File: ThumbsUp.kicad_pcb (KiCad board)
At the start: 2 copper layers, 395.5 x 277.7 mm, 210 parts, among them IC1 RP2040, IC2 W25Q128JVSIM, IC3 RP2040, IC4 W25Q128JVSIM, J1 Conn_01x04_Male, J10 Raiser_Male, J11 Raiser_Female, J12 Raiser_Male, J13 Raiser_Female, J14 Raiser_Male, J15 Raiser_Female, J16 Raiser_Male, J17 Raiser_Female, J18 Raiser_Male, J19 Raiser_Female, J2 Conn_01x04_Male, J20 Conn_01x04_Female, J21 Conn_01x04_Female, J22 Conn_01x04_Female, J23 Conn_01x04_Female, J24 Conn_01x04_Male, J25 Conn_01x04_Male, J26 Conn_01x04_Male, J27 Conn_01x04_Male, J28 Conn_01x04_Female, J29 Conn_01x04_Female, J3 Conn_01x04_Female, J30 Conn_01x04_Female, J31 Conn_01x04_Female, J32 USB_C_Receptacle_USB2.0, J33 Raiser_Male, J34 Raiser_Female, J35 Raiser_Male, J36 PJ-3200B, J37 USB_C_Receptacle_USB2.0, J38 Raiser_Female, J39 Raiser_Male, J4 Conn_01x04_Male, J40 Raiser_Female, J41 Raiser_Male, J42 Raiser_Female, J43 Raiser_Male, J44 Raiser_Female, J45 Raiser_Male, J46 PJ-3200B, J47 Raiser_Female, J48 Raiser_Male, J49 Raiser_Female, J5 Conn_01x04_Female, J50 Raiser_Male, J51 Raiser_Female, J52 Raiser_Male, J55 Conn_01x04_Male, J6 Conn_01x04_Male, J7 Conn_01x04_Male, J8 Conn_01x04_Male, J9 Raiser_Female, U1 AMS1117-3.3_SOT223, U2 AMS1117-3.3_SOT223, Y1 ABLS-12.000MHZ-B4-T, Y2 ABLS-12.000MHZ-B4-T

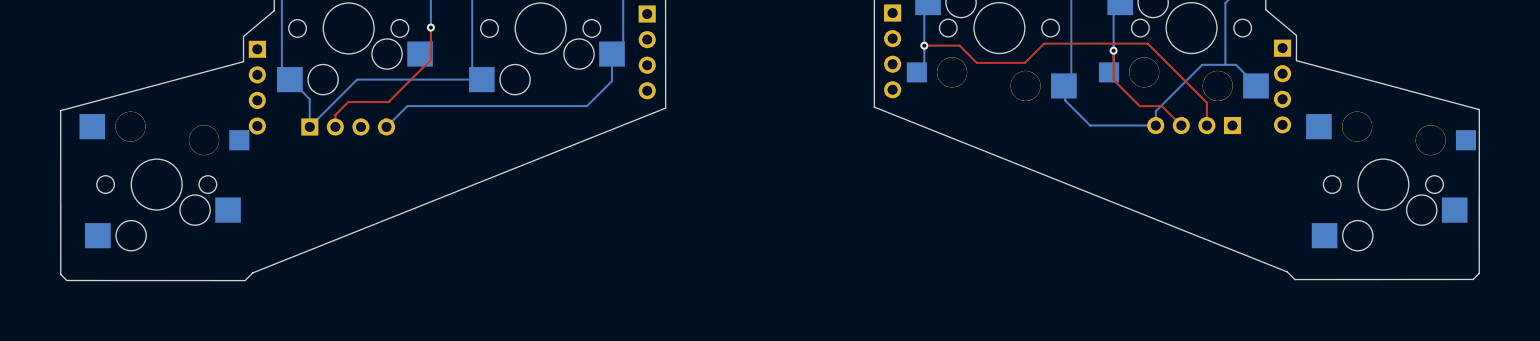
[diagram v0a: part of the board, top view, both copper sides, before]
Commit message: Adding the 3key thumbclusters
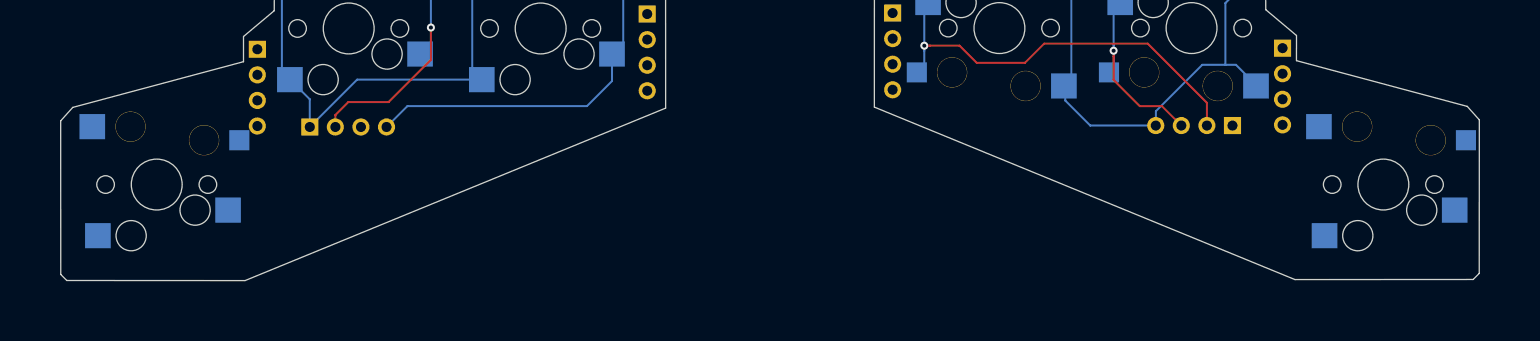
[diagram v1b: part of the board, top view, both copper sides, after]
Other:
- outline, holes or cut-outs redrawn
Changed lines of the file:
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@@
     (aux_axis_origin 0 0)
     (grid_origin 166.8 443.6)
-    (visible_elements 7FFFFFFF)
+    (visible_elements 7FFFF7FF)
     (pcbplotparams
       (layerselection 0x010fc_ffffffff)
@@
     )
   )
+  (gr_line (start 21.830195 401.078102) (end 23.030195 402.418102) (layer Edge.Cuts) (width 0.05))
+  (gr_line (start 23.030195 402.418102) (end 23.020195 417.668102) (layer Edge.Cuts) (width 0.05))
+  (gr_line (start 4.870195 396.538102) (end 21.830195 401.078102) (layer Edge.Cuts) (width 0.05))
+  (gr_line (start -116.66 401.18) (end -117.86 402.52) (layer Edge.Cuts) (width 0.05))
   (gr_line (start -38.149804 456.568103) (end -53.129804 456.558103) (layer Edge.Cuts) (width 0.05))
   (gr_line (start -53.849804 457.278103) (end -53.849804 474.838103) (layer Edge.Cuts) (width 0.05))
@@
   (gr_line (start -87.96 456.67) (end -72.98 456.66) (layer Edge.Cuts) (width 0.05))
   (gr_line (start -88.423847 456.271308) (end -87.96 456.67) (layer Edge.Cuts) (width 0.05))
-  (gr_line (start -37.051253 401.149426) (end 3.960195 417.518102) (layer Edge.Cuts) (width 0.05))
+  (gr_line (start -37.051253 401.149426) (end 4.720195 418.278102) (layer Edge.Cuts) (width 0.05))
   (gr_line (start 4.870195 396.538102) (end 4.871005 394.036601) (layer Edge.Cuts) (width 0.05))
-  (gr_line (start 4.720195 418.278102) (end 3.960195 417.518102) (layer Edge.Cuts) (width 0.05))
   (gr_line (start 23.020195 417.668102) (end 22.420195 418.268102) (layer Edge.Cuts) (width 0.05))
   (gr_line (start 22.420195 418.268102) (end 4.720195 418.278102) (layer Edge.Cuts) (width 0.05))
-  (gr_line (start 23.030195 401.398102) (end 23.020195 417.668102) (layer Edge.Cuts) (width 0.05))
-  (gr_line (start 4.870195 396.538102) (end 23.030195 401.398102) (layer Edge.Cuts) (width 0.05))
-  (gr_line (start -99.55 418.38) (end -98.79 417.62) (layer Edge.Cuts) (width 0.05))
   (gr_line (start -117.25 418.37) (end -99.55 418.38) (layer Edge.Cuts) (width 0.05))
   (gr_line (start -117.85 417.77) (end -117.25 418.37) (layer Edge.Cuts) (width 0.05))
-  (gr_line (start -117.86 401.5) (end -117.85 417.77) (layer Edge.Cuts) (width 0.05))
-  (gr_line (start -99.7 396.64) (end -117.86 401.5) (layer Edge.Cuts) (width 0.05))
+  (gr_line (start -117.86 402.52) (end -117.85 417.77) (layer Edge.Cuts) (width 0.05))
+  (gr_line (start -99.7 396.64) (end -116.66 401.18) (layer Edge.Cuts) (width 0.05))
   (gr_line (start -25.711253 364.399426) (end -24.111253 362.799426) (layer Edge.Cuts) (width 0.05))
   (gr_line (start -24.111253 362.799426) (end -21.211253 352.699426) (layer Edge.Cuts) (width 0.05))
@@
   (gr_line (start -57.778552 401.251324) (end -57.783847 390.111308) (layer Edge.Cuts) (width 0.05))
   (gr_line (start -37.051253 401.149426) (end -37.045957 390.009411) (layer Edge.Cuts) (width 0.05))
-  (gr_line (start -57.778552 401.251324) (end -98.79 417.62) (layer Edge.Cuts) (width 0.05))
+  (gr_line (start -57.778552 401.251324) (end -99.55 418.38) (layer Edge.Cuts) (width 0.05))
   (gr_line (start 0.248753 386.05148) (end 1.806995 387.552472) (layer Edge.Cuts) (width 0.05))
   (gr_line (start -34.157244 386.17596) (end -32.251197 379.110269) (layer Edge.Cuts) (width 0.05))

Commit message: Tracedd the 3key thumbclusters
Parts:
- removed the J10 at (-129.0, 461.6)
- removed the J10 at (-98.3, 395.4)
- removed the J10 at (-87.5, 342.2)
- removed the J14 at (-90.2, 458.1)
- removed the J14 at (-59.6, 391.9)
- removed the J14 at (-48.8, 338.7)
- removed the J18 at (-102.8, 447.6)
- removed the J18 at (-72.2, 381.4)
- removed the J18 at (-61.4, 328.2)
- removed the J33 at (2.85, 461.5)
- removed the J33 at (3.49, 395.3)
- removed the J33 at (-4.68, 342.1)
- removed the J35 at (-23.3, 447.5)
- removed the J35 at (-22.7, 381.3)
- removed the J35 at (-30.9, 328.2)
- removed the J4 at (-123.8, 469.3)
- removed the J4 at (-93.1, 403.1)
- removed the J48 at (-35.9, 458.0)
- removed the J48 at (-35.2, 391.8)
- removed the J48 at (-43.4, 338.7)
- removed the J6 at (-2.12, 469.1)
- removed the J6 at (-1.48, 403.0)
- removed the J6 at (-9.65, 349.8)
- removed the MX18 at (-100.8, 459.5)
- removed the MX18 at (-70.2, 393.3)
- removed the MX18 at (-59.4, 337.0)
- removed the MX22 at (-119.9, 459.5)
- removed the MX22 at (-89.3, 393.3)
- removed the MX22 at (-78.5, 340.1)
- removed the MX26 at (-6.23, 459.5)
- removed the MX26 at (-5.55, 393.3)
- removed the MX26 at (-13.6, 340.2)
- removed the MX30 at (-25.3, 459.5)
- removed the MX30 at (-24.6, 393.3)
- removed the MX30 at (-32.7, 337.0)
- added J53: Conn_01x04_Male, Connector_PinHeader_2.54mm:PinHeader_1x04_P2.54mm_Vertical, B.Cu at (-93.1, 403.1)
- added J54: Conn_01x04_Male, Connector_PinHeader_2.54mm:PinHeader_1x04_P2.54mm_Vertical, B.Cu at (-123.8, 469.3)
- added J56: Conn_01x04_Male, Connector_PinHeader_2.54mm:PinHeader_1x04_P2.54mm_Vertical, B.Cu at (-1.48, 403.0)
- added J57: Conn_01x04_Male, Connector_PinHeader_2.54mm:PinHeader_1x04_P2.54mm_Vertical, B.Cu at (-2.12, 469.1)
- added J58: Conn_01x04_Male, Connector_PinHeader_2.54mm:PinHeader_1x04_P2.54mm_Vertical, B.Cu at (-9.65, 349.8)
- added J59: Raiser_Male, Connector_PinHeader_2.54mm:PinHeader_1x04_P2.54mm_Vertical, B.Cu at (-87.5, 342.2)
- added J60: Raiser_Male, Connector_PinHeader_2.54mm:PinHeader_1x04_P2.54mm_Vertical, B.Cu at (-61.4, 328.2)
- added J61: Raiser_Male, Connector_PinHeader_2.54mm:PinHeader_1x04_P2.54mm_Vertical, B.Cu at (-48.8, 338.7)
- added J62: Raiser_Male, Connector_PinHeader_2.54mm:PinHeader_1x04_P2.54mm_Vertical, B.Cu at (-43.4, 338.7)
- added J63: Raiser_Male, Connector_PinHeader_2.54mm:PinHeader_1x04_P2.54mm_Vertical, B.Cu at (-30.9, 328.2)
- added J64: Raiser_Male, Connector_PinHeader_2.54mm:PinHeader_1x04_P2.54mm_Vertical, B.Cu at (-4.68, 342.1)
- added J65: Raiser_Male, Connector_PinHeader_2.54mm:PinHeader_1x04_P2.54mm_Vertical, B.Cu at (-98.3, 395.4)
- added J66: Raiser_Male, Connector_PinHeader_2.54mm:PinHeader_1x04_P2.54mm_Vertical, B.Cu at (-72.2, 381.4)
- added J67: Raiser_Male, Connector_PinHeader_2.54mm:PinHeader_1x04_P2.54mm_Vertical, B.Cu at (-59.6, 391.9)
- added J68: Raiser_Male, Connector_PinHeader_2.54mm:PinHeader_1x04_P2.54mm_Vertical, B.Cu at (-35.2, 391.8)
- added J69: Raiser_Male, Connector_PinHeader_2.54mm:PinHeader_1x04_P2.54mm_Vertical, B.Cu at (-22.7, 381.3)
- added J70: Raiser_Male, Connector_PinHeader_2.54mm:PinHeader_1x04_P2.54mm_Vertical, B.Cu at (3.49, 395.3)
- added J71: Raiser_Male, Connector_PinHeader_2.54mm:PinHeader_1x04_P2.54mm_Vertical, B.Cu at (-129.0, 461.6)
- added J72: Raiser_Male, Connector_PinHeader_2.54mm:PinHeader_1x04_P2.54mm_Vertical, B.Cu at (-102.8, 447.6)
- added J73: Raiser_Male, Connector_PinHeader_2.54mm:PinHeader_1x04_P2.54mm_Vertical, B.Cu at (-90.2, 458.1)
- added J74: Raiser_Male, Connector_PinHeader_2.54mm:PinHeader_1x04_P2.54mm_Vertical, B.Cu at (-35.9, 458.0)
- added J75: Raiser_Male, Connector_PinHeader_2.54mm:PinHeader_1x04_P2.54mm_Vertical, B.Cu at (-23.3, 447.5)
- added J76: Raiser_Male, Connector_PinHeader_2.54mm:PinHeader_1x04_P2.54mm_Vertical, B.Cu at (2.85, 461.5)
- added MX57: SwThL, keyswitches:MX-GLP2-HotSwap, F.Cu at (69.1, 354.5)
- added MX58: SwThR, keyswitches:MX-GLP2-HotSwap, F.Cu at (228.3, 352.1)
- added MX59: SwLSHFT, keyswitches:MX-GLP2-HotSwap, F.Cu at (-89.3, 393.3)
- added MX60: SwLSHFT, keyswitches:MX-GLP2-HotSwap, F.Cu at (-119.9, 459.5)
- added MX61: SwLSHFT, keyswitches:MX-GLP2-HotSwap, F.Cu at (-78.5, 340.1)
- added MX62: SwLMOD, keyswitches:MX-GLP2-HotSwap, F.Cu at (-70.2, 393.3)
- added MX63: SwLMOD, keyswitches:MX-GLP2-HotSwap, F.Cu at (-100.8, 459.5)
- added MX64: SwLMOD, keyswitches:MX-GLP2-HotSwap, F.Cu at (-59.4, 337.0)
- added MX71: SwRMOD, keyswitches:MX-GLP2-HotSwap, F.Cu at (-24.6, 393.3)
- added MX72: SwRMOD, keyswitches:MX-GLP2-HotSwap, F.Cu at (-25.3, 459.5)
- added MX73: SwRMOD, keyswitches:MX-GLP2-HotSwap, F.Cu at (-32.7, 337.0)
- added MX74: SwRSHFT, keyswitches:MX-GLP2-HotSwap, F.Cu at (-5.55, 393.3)
- added MX75: SwRSHFT, keyswitches:MX-GLP2-HotSwap, F.Cu at (-6.23, 459.5)
- added MX76: SwRSHFT, keyswitches:MX-GLP2-HotSwap, F.Cu at (-13.6, 340.2)
- moved C20 0.07 mm to (166.6, 460.1)
- moved C26 0.07 mm to (166.6, 459.1)
- renumbered MX57 to MX65, MX57 to MX66, MX57 to MX67, MX58 to MX68, MX58 to MX69, MX58 to MX70
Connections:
- J10 pad 1: Net-(J10-Pad1) -> (no net)
- J10 pad 2: Net-(J10-Pad2) -> (no net)
- J10 pad 3: Net-(J10-Pad3) -> (no net)
- J10 pad 4: Net-(J10-Pad4) -> (no net)
- J14 pad 1: Net-(J14-Pad1) -> (no net)
- J14 pad 2: Net-(J14-Pad2) -> (no net)
- J14 pad 3: Net-(J14-Pad3) -> (no net)
- J14 pad 4: Net-(J14-Pad4) -> (no net)
- J18 pad 1: Net-(J18-Pad1) -> (no net)
- J18 pad 2: Net-(J18-Pad2) -> (no net)
- J18 pad 3: Net-(J18-Pad3) -> (no net)
- J18 pad 4: Net-(J18-Pad4) -> (no net)
- J33 pad 1: Net-(J33-Pad1) -> (no net)
- J33 pad 2: Net-(J33-Pad2) -> (no net)
- J33 pad 3: Net-(J33-Pad3) -> (no net)
- J33 pad 4: Net-(J33-Pad4) -> (no net)
- J35 pad 1: Net-(J35-Pad1) -> (no net)
- J35 pad 2: Net-(J35-Pad2) -> (no net)
- J35 pad 3: Net-(J35-Pad3) -> (no net)
- J35 pad 4: Net-(J35-Pad4) -> (no net)
- J48 pad 1: Net-(J48-Pad1) -> (no net)
- J48 pad 2: Net-(J48-Pad2) -> (no net)
- J48 pad 3: Net-(J48-Pad3) -> (no net)
- J48 pad 4: Net-(J48-Pad4) -> (no net)
- J55 pad 1: Net-(J4-Pad1) -> Net-(J55-Pad1)
- J55 pad 2: Net-(J4-Pad2) -> Net-(J55-Pad2)
- J55 pad 3: Net-(J4-Pad3) -> Net-(J55-Pad3)
- J55 pad 4: Net-(J4-Pad4) -> Net-(J55-Pad4)
- MX65 pad 1: Net-(J4-Pad1) -> Net-(J53-Pad1)
- MX65 pad 2: Net-(J4-Pad3) -> Net-(J53-Pad3)
- MX66 pad 1: Net-(J4-Pad1) -> Net-(J54-Pad1)
- MX66 pad 2: Net-(J4-Pad3) -> Net-(J54-Pad3)
- MX67 pad 1: Net-(J4-Pad1) -> Net-(J55-Pad1)
- MX67 pad 2: Net-(J4-Pad3) -> Net-(J55-Pad3)
- MX68 pad 1: Net-(J6-Pad4) -> Net-(J56-Pad4)
- MX68 pad 2: Net-(J6-Pad1) -> Net-(J56-Pad1)
- MX69 pad 1: Net-(J6-Pad4) -> Net-(J57-Pad4)
- MX69 pad 2: Net-(J6-Pad1) -> Net-(J57-Pad1)
- MX70 pad 1: Net-(J6-Pad4) -> Net-(J58-Pad4)
- MX70 pad 2: Net-(J6-Pad1) -> Net-(J58-Pad1)
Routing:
- net Net-(J4-Pad1): track 224.1 -> 59.2 mm, vias 2 -> 0
- net Net-(J6-Pad4): track 217.6 -> 58.2 mm
- net Net-(J6-Pad2): track 166.5 -> 41.7 mm, vias 4 -> 1
- net Net-(J4-Pad4): track 125.7 -> 34.4 mm, vias 1 -> 0
- net Net-(J53-Pad1): track 0.00 -> 83.4 mm
- net Net-(J54-Pad1): track 0.00 -> 82.6 mm, vias 0 -> 2
- net Net-(J57-Pad4): track 0.00 -> 81.5 mm
- net Net-(J55-Pad1): track 0.00 -> 79.5 mm, vias 0 -> 2
- net Net-(J58-Pad4): track 0.00 -> 76.2 mm
- net Net-(J4-Pad2): track 94.2 -> 23.6 mm, vias 4 -> 1
- net Net-(J56-Pad4): track 0.00 -> 67.6 mm
- net Net-(J57-Pad1): track 0.00 -> 59.8 mm, vias 0 -> 2
- net Net-(J6-Pad3): track 76.8 -> 18.9 mm, vias 4 -> 1
- net Net-(J54-Pad3): track 0.00 -> 55.9 mm, vias 0 -> 1
- net Net-(J57-Pad2): track 0.00 -> 41.7 mm, vias 0 -> 1
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
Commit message: Put the silkscreens on, ready for Gerbers creation
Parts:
- added G***: LOGO, Silkscreens:Crowfeet75, B.Cu at (138.4, 567.7)
- added G***: LOGO, Silkscreens:Crowfeet75, F.Cu at (-145.4, 409.6)
- added G***: LOGO, Silkscreens:Crowfeet75, F.Cu at (141.0, 404.6)
- added G***: LOGO, Silkscreens:Crowfeet75, F.Cu at (138.5, 564.2)
- moved MX64 49.9 mm to (-106.8, 352.4)
- moved MX67 49.9 mm to (-106.8, 371.5)
- moved J55 49.9 mm to (-129.8, 365.3)
- moved J60 49.9 mm to (-108.9, 343.7)
- moved J61 49.9 mm to (-96.3, 354.1)
- moved J63 49.9 mm to (-78.3, 343.6)
- moved MX61 49.9 mm to (-125.9, 355.6)
- moved MX70 49.9 mm to (-80.1, 371.5)
- moved MX73 49.9 mm to (-80.1, 352.4)
- moved J62 49.9 mm to (-90.8, 354.1)
- moved J58 49.9 mm to (-57.1, 365.3)
- moved J59 49.9 mm to (-135.0, 357.6)
- moved J64 49.9 mm to (-52.1, 357.6)
- moved MX76 49.9 mm to (-61.0, 355.6)
- moved MX59 48.9 mm to (-136.2, 407.3)
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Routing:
- net Net-(J23-Pad3): track 41.2 -> 42.3 mm
- net Net-(J15-Pad3): track 96.9 -> 98.0 mm
- net Net-(J44-Pad4): track 69.5 -> 68.6 mm
- net Net-(J44-Pad2): track 102.6 -> 101.8 mm
- net Net-(J44-Pad1): track 136.5 -> 135.7 mm
- net Net-(J44-Pad3): track 79.0 -> 78.4 mm
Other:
- board size 395.5 x 277.7 mm -> 429.9 x 270.5 mm

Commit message: Gerber files generated
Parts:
- moved G*** 3.95 mm to (140.5, 564.3)

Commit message: Updated BOMs, Gerbers.
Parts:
- removed G*** (x4): LOGO, Silkscreens:Crowfeet75
- removed MX57: SwThL, keyswitches:MX-GLP2-HotSwap
- removed MX58: SwThR, keyswitches:MX-GLP2-HotSwap
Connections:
- J4 pad 3: Net-(J4-Pad3) -> (no net)
- J6 pad 1: Net-(J6-Pad1) -> (no net)
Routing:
- net Net-(J4-Pad1): track 59.2 -> 48.2 mm
- net Net-(J6-Pad4): track 58.2 -> 47.1 mm
- net Net-(J6-Pad1): track 7.40 -> 0.00 mm
- net Net-(J4-Pad3): track 7.40 -> 0.00 mm
